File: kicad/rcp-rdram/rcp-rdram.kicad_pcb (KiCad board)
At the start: 2 copper layers, 47.1 x 49.7 mm, 32 parts, among them P1 RDRAM-EDGE, U11 RDRAM18-NUS, U11-2 RDRAM18-NUS, U14 RDRAM18-NUS, U14-2 RDRAM18-NUS, U15 MX8330, X2 14.705MHz

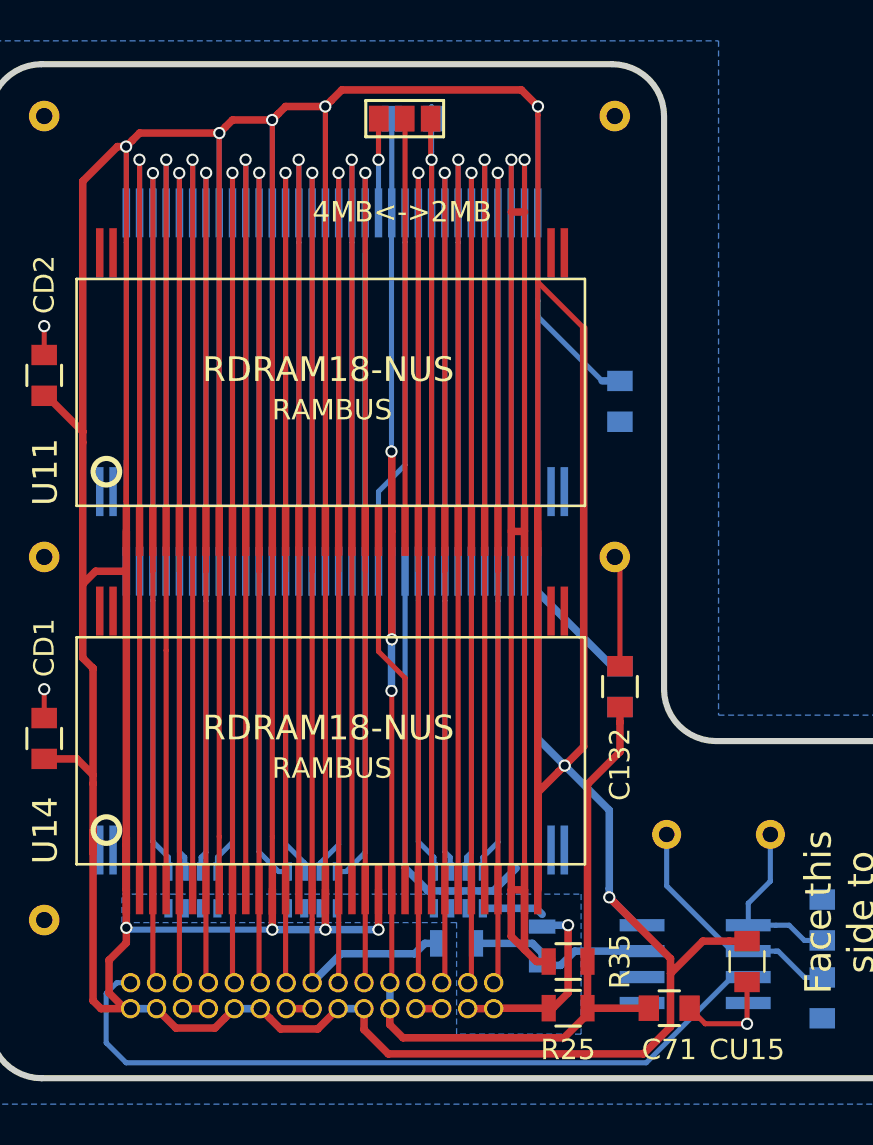
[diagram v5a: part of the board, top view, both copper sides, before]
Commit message: Tuned power track width to 0.37mm whenever possible
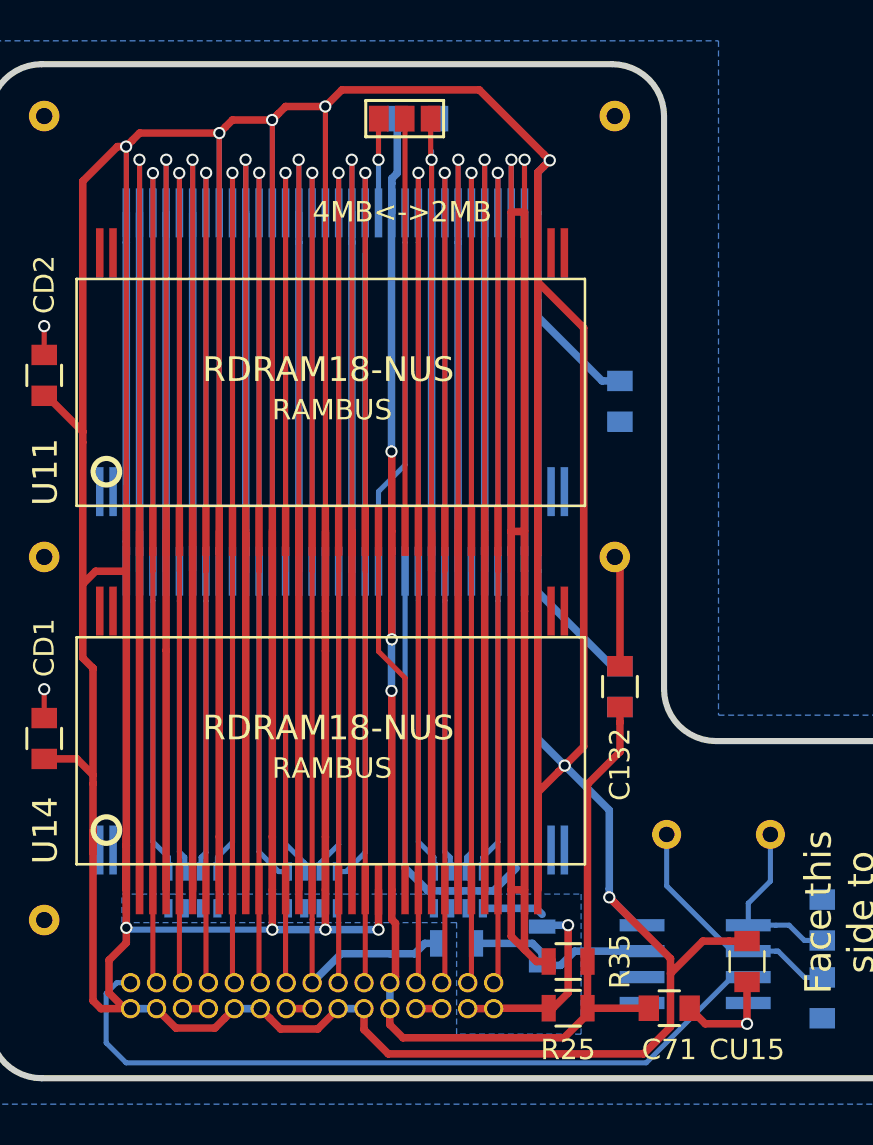
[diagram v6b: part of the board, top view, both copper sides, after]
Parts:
- moved C133 0.25 mm to (43.8, 20.4)
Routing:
- net GND: track 672.5 -> 668.0 mm
- net VDD: track 514.8 -> 511.7 mm

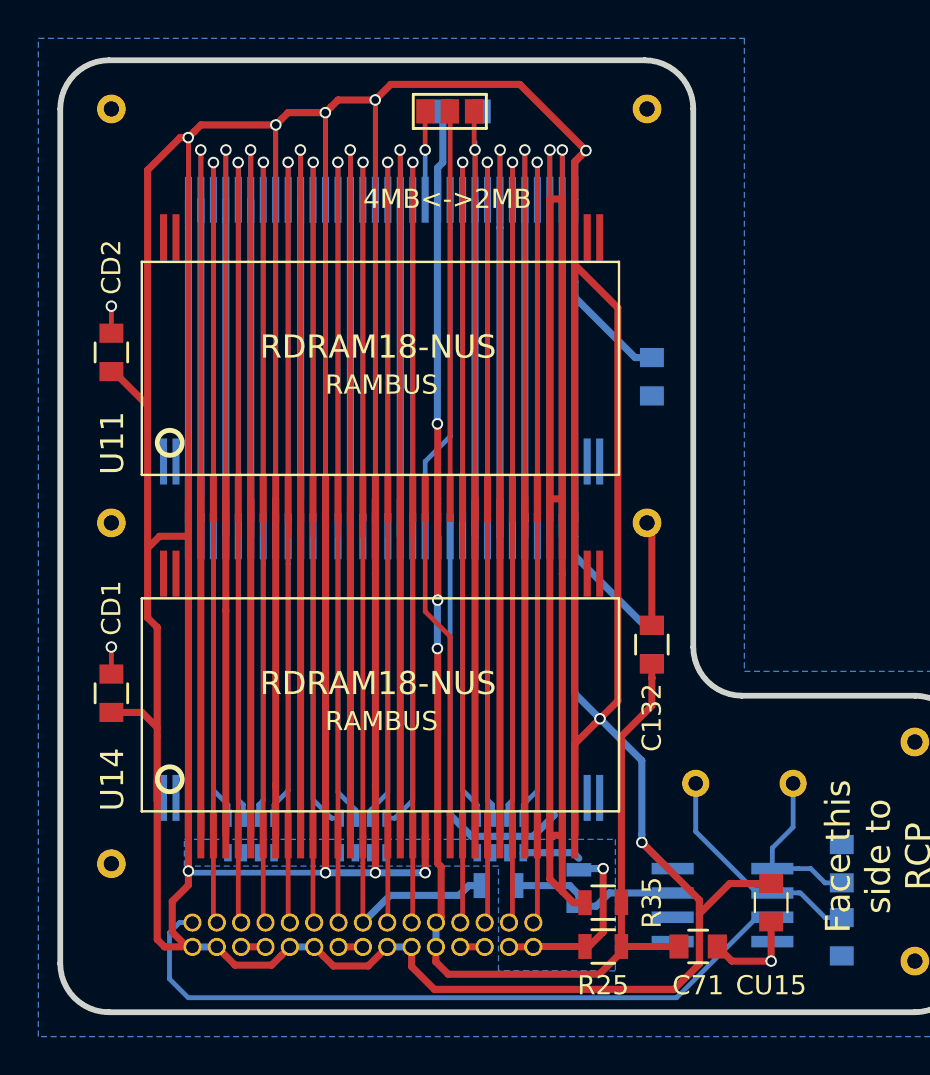
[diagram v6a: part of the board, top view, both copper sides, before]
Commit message: More stitchings for VREF line, minor text cleanups
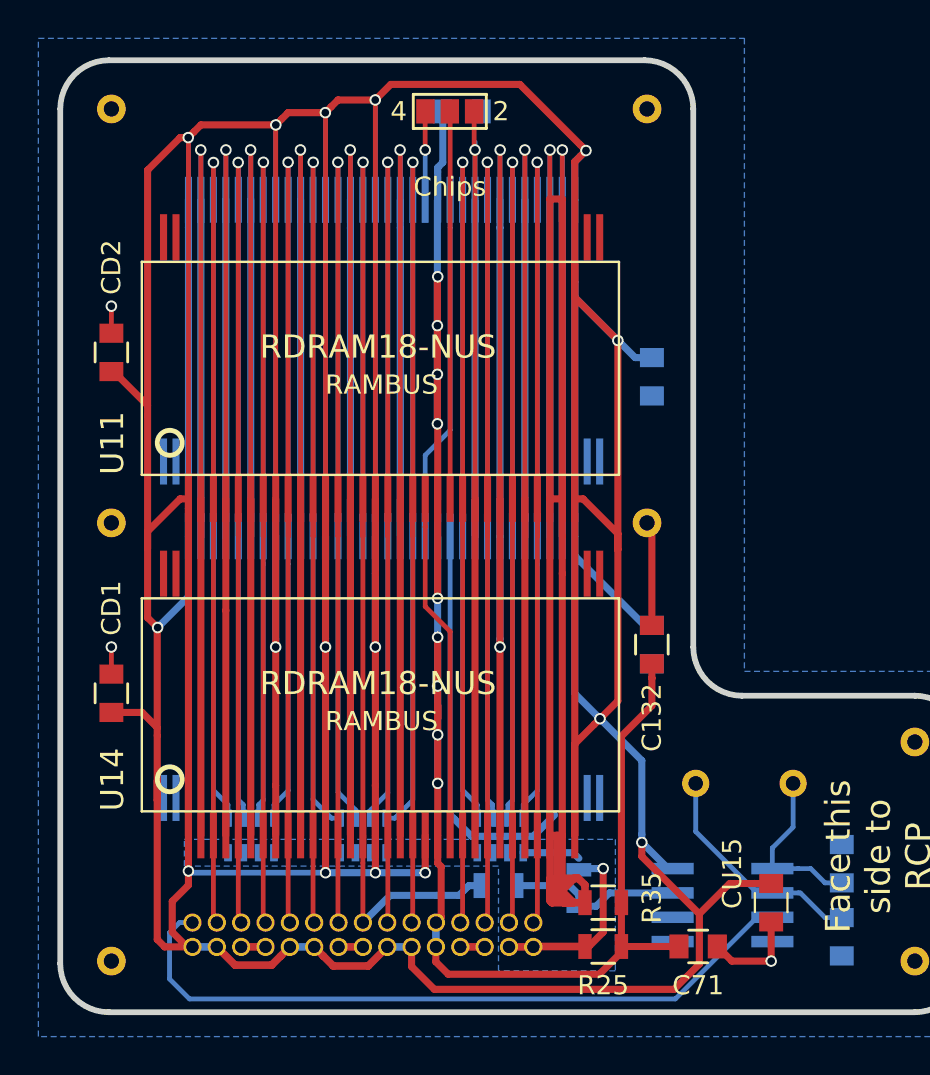
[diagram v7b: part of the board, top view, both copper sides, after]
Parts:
- moved REF** 5.08 mm to (25.5, 64.8)
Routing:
- net VDD: track 511.7 -> 537.6 mm, vias 11 -> 16
- net /VREF: track 77.3 -> 95.4 mm, vias 3 -> 9
- net GND: track 668.0 -> 685.7 mm, vias 14 -> 15
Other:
- board text added: "2"
- board text added: "4"
- board text added: "Chips"
- board text removed: "4MB<->2MB"

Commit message: Minor cleanups
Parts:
- moved C71 6.48 mm to (56.0, 70.5)
- moved R25 6.48 mm to (51.1, 70.5)
- moved REF** 6.48 mm to (67.3, 71.2)
- moved REF** 6.48 mm to (25.4, 71.2)
- moved C132 6.48 mm to (53.6, 54.7)
- moved CD1 6.48 mm to (25.4, 57.3)
- moved CU15 6.48 mm to (59.8, 68.2)
- moved JP1 6.48 mm to (43.1, 26.9)
- moved R35 6.48 mm to (51.1, 68.2)
- moved REF** 6.48 mm to (25.4, 26.8)
- moved REF** 6.48 mm to (25.4, 48.4)
- moved REF** 6.48 mm to (53.3, 26.8)
- moved REF** 6.48 mm to (53.3, 48.4)
- moved U11 6.48 mm to (39.5, 41.2)
- moved U14 6.48 mm to (39.5, 58.7)
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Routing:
- net GND: track 685.7 -> 695.0 mm, vias 15 -> 17
- net /VTERM: track 12.9 -> 14.2 mm
